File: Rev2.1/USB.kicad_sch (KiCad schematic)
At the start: 17 parts, among them J10 Conn_01x08_Pin, J8 USB_OTG, P1 USB_C_Plug_USB2.0, U5 MCP2200T-I-SO, U6 STMPS2151STR(Current protecti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, U7 USBLC6-2P6(ESD protection), Y1 12MHz

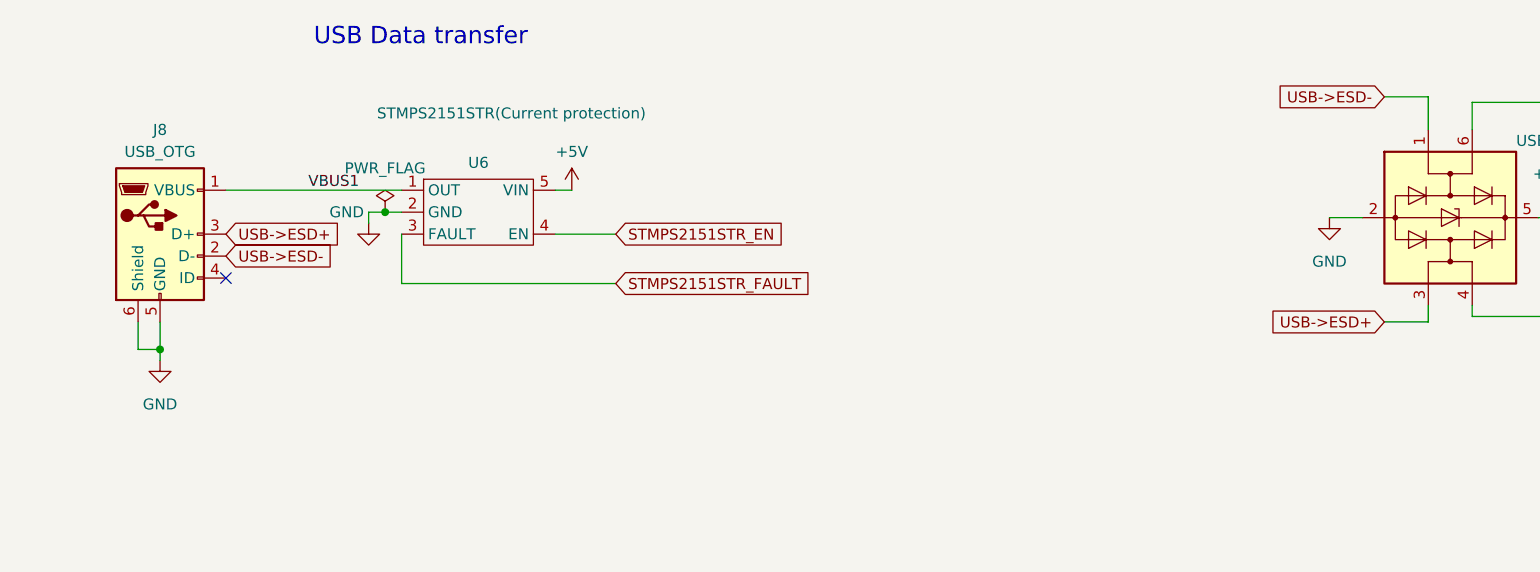
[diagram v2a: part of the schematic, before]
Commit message: finished the first mock up of routing now just need to polish it up
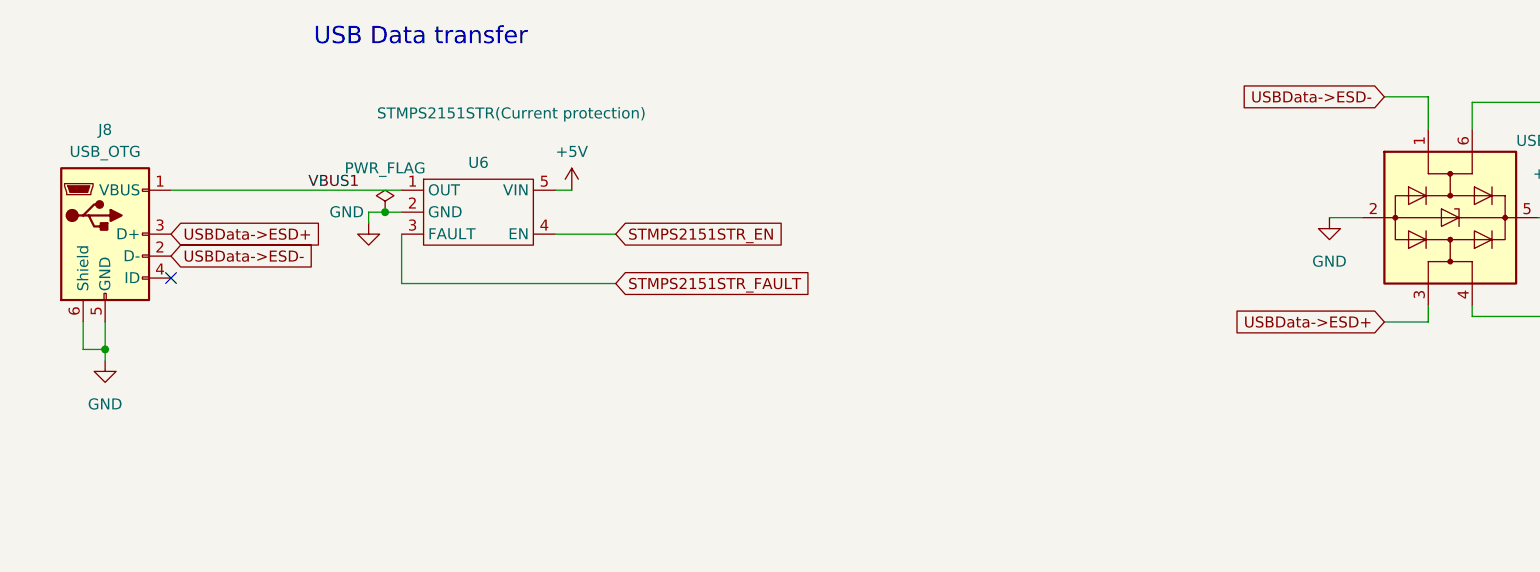
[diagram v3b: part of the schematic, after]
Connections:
- net USB->ESD+: no longer J8.3 (D+), U7.3 (I/O2)
- net USB->ESD-: no longer J8.2 (D-), U7.1 (I/O1)
- new net USBData->ESD+: J8.3 (D+), U7.3 (I/O2)
- new net USBData->ESD-: J8.2 (D-), U7.1 (I/O1)
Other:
- moved on the sheet: J8
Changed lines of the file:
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@@
   (junction (at 54.61 38.1) (diameter 0) (color 0 0 0 0)
   )
-  (junction (at 28.575 53.975) (diameter 0) (color 0 0 0 0)
+  (junction (at 22.225 53.975) (diameter 0) (color 0 0 0 0)
   )
   (junction (at 218.44 96.52) (diameter 0) (color 0 0 0 0)
   )
   (no_connect (at 55.245 120.015))
-  (no_connect (at 36.195 45.72))
+  (no_connect (at 29.845 45.72))
   (wire (pts (xy 52.705 39.37) (xy 52.705 38.1))
     (stroke (width 0) (type default))
@@
     (stroke (width 0) (type default))
   )
-  (wire (pts (xy 28.575 55.245) (xy 28.575 53.975))
+  (wire (pts (xy 22.225 55.245) (xy 22.225 53.975))
     (stroke (width 0) (type default))
   )
@@
     (stroke (width 0) (type default))
   )
-  (wire (pts (xy 28.575 53.975) (xy 28.575 50.8))
+  (wire (pts (xy 22.225 53.975) (xy 22.225 50.8))
     (stroke (width 0) (type default))
   )
@@
     (stroke (width 0) (type default))
   )
-  (wire (pts (xy 26.035 53.975) (xy 28.575 53.975))
+  (wire (pts (xy 19.685 53.975) (xy 22.225 53.975))
     (stroke (width 0) (type default))
   )
@@
     (stroke (width 0) (type default))
   )
-  (wire (pts (xy 56.515 35.56) (xy 36.195 35.56))
+  (wire (pts (xy 56.515 35.56) (xy 29.845 35.56))
     (stroke (width 0) (type default))
   )
-  (wire (pts (xy 26.035 50.8) (xy 26.035 53.975))
+  (wire (pts (xy 19.685 50.8) (xy 19.685 53.975))
     (stroke (width 0) (type default))
   )
@@
     (effects (font (size 1.27 1.27)) (justify left bottom))
   )
-  (global_label "USB->ESD+" (shape input) (at 170.18 50.8 180) (fields_autoplaced)
-    (effects (font (size 1.27 1.27)) (justify right))
-    (property "Intersheetrefs" "${INTERSHEET_REFS}" (at 155.0391 50.8 0)
-      (effects (font (size 1.27 1.27)) (justify right) hide)
-    )
-  )
   (global_label "USB_PROG+" (shape input) (at 128.905 144.78 0) (fields_autoplaced)
     (effects (font (size 1.27 1.27)) (justify left))
@@
     )
   )
+  (global_label "USBData->ESD-" (shape input) (at 170.18 24.765 180) (fields_autoplaced)
+    (effects (font (size 1.27 1.27)) (justify right))
+    (property "Intersheetrefs" "${INTERSHEET_REFS}" (at 150.7454 24.765 0)
+      (effects (font (size 1.27 1.27)) (justify right) hide)
+    )
+  )
   (global_label "GP3" (shape input) (at 36.195 180.34 0) (fields_autoplaced)
     (effects (font (size 1.27 1.27)) (justify left))
@@
     )
   )
-  (global_label "USB->ESD-" (shape input) (at 36.195 43.18 0) (fields_autoplaced)
+  (global_label "USBData->ESD-" (shape input) (at 29.845 43.18 0) (fields_autoplaced)
     (effects (font (size 1.27 1.27)) (justify left))
-    (property "Intersheetrefs" "${INTERSHEET_REFS}" (at 51.3359 43.18 0)
+    (property "Intersheetrefs" "${INTERSHEET_REFS}" (at 49.2796 43.18 0)
       (effects (font (size 1.27 1.27)) (justify left) hide)
     )
@@
     )
   )
-  (global_label "USB->ESD-" (shape input) (at 170.18 24.765 180) (fields_autoplaced)
-    (effects (font (size 1.27 1.27)) (justify right))
-    (property "Intersheetrefs" "${INTERSHEET_REFS}" (at 155.0391 24.765 0)
-      (effects (font (size 1.27 1.27)) (justify right) hide)
-    )
-  )
   (global_label "STMPS2151STR_EN" (shape input) (at 81.28 40.64 0) (fields_autoplaced)
     (effects (font (size 1.27 1.27)) (justify left))
@@
     )
   )
-  (global_label "USB->ESD+" (shape input) (at 36.195 40.64 0) (fields_autoplaced)
+  (global_label "USBData->ESD+" (shape input) (at 29.845 40.64 0) (fields_autoplaced)
     (effects (font (size 1.27 1.27)) (justify left))
-    (property "Intersheetrefs" "${INTERSHEET_REFS}" (at 51.3359 40.64 0)
+    (property "Intersheetrefs" "${INTERSHEET_REFS}" (at 49.2796 40.64 0)
       (effects (font (size 1.27 1.27)) (justify left) hide)
     )
@@
     )
   )
+  (global_label "USBData->ESD+" (shape input) (at 170.18 50.8 180) (fields_autoplaced)
+    (effects (font (size 1.27 1.27)) (justify right))
+    (property "Intersheetrefs" "${INTERSHEET_REFS}" (at 150.7454 50.8 0)
+      (effects (font (size 1.27 1.27)) (justify right) hide)
+    )
+  )
   (symbol (lib_id "power:GND") (at 259.08 147.32 0) (unit 1)
     (in_bom yes) (on_board yes) (dnp no) (fields_autoplaced)
@@
     )
   )
-  (symbol (lib_id "power:GND") (at 28.575 55.245 0) (unit 1)
+  (symbol (lib_id "power:GND") (at 22.225 55.245 0) (unit 1)
     (in_bom yes) (on_board yes) (dnp no) (fields_autoplaced)
-    (property "Reference" "#PWR047" (at 28.575 61.595 0)
+    (property "Reference" "#PWR047" (at 22.225 61.595 0)
       (effects (font (size 1.27 1.27)) hide)
     )
-    (property "Value" "GND" (at 28.575 60.325 0)
+    (property "Value" "GND" (at 22.225 60.325 0)
       (effects (font (size 1.27 1.27)))
     )
-    (property "Footprint" "" (at 28.575 55.245 0)
+    (property "Footprint" "" (at 22.225 55.245 0)
       (effects (font (size 1.27 1.27)) hide)
     )
-    (property "Datasheet" "" (at 28.575 55.245 0)
+    (property "Datasheet" "" (at 22.225 55.245 0)
       (effects (font (size 1.27 1.27)) hide)
     )
@@
     )
   )
-  (symbol (lib_id "Connector:USB_OTG") (at 28.575 40.64 0) (unit 1)
+  (symbol (lib_id "Connector:USB_OTG") (at 22.225 40.64 0) (unit 1)
     (in_bom yes) (on_board yes) (dnp no) (fields_autoplaced)
-    (property "Reference" "J8" (at 28.575 28.575 0)
+    (property "Reference" "J8" (at 22.225 28.575 0)
       (effects (font (size 1.27 1.27)))
     )
-    (property "Value" "USB_OTG" (at 28.575 31.115 0)
+    (property "Value" "USB_OTG" (at 22.225 31.115 0)
       (effects (font (size 1.27 1.27)))
     )
-    (property "Footprint" "Connector_USB:USB_Mini-B_Wuerth_65100516121_Horizontal" (at 32.385 41.91 0)
+    (property "Footprint" "Connector_USB:USB_Mini-B_Wuerth_65100516121_Horizontal" (at 26.035 41.91 0)
       (effects (font (size 1.27 1.27)) hide)
     )
-    (property "Datasheet" " ~" (at 32.385 41.91 0)
+    (property "Datasheet" " ~" (at 26.035 41.91 0)
       (effects (font (size 1.27 1.27)) hide)
     )
